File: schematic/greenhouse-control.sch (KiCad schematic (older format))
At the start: 10 parts, among them Q1 BC547, U1 PCF8574

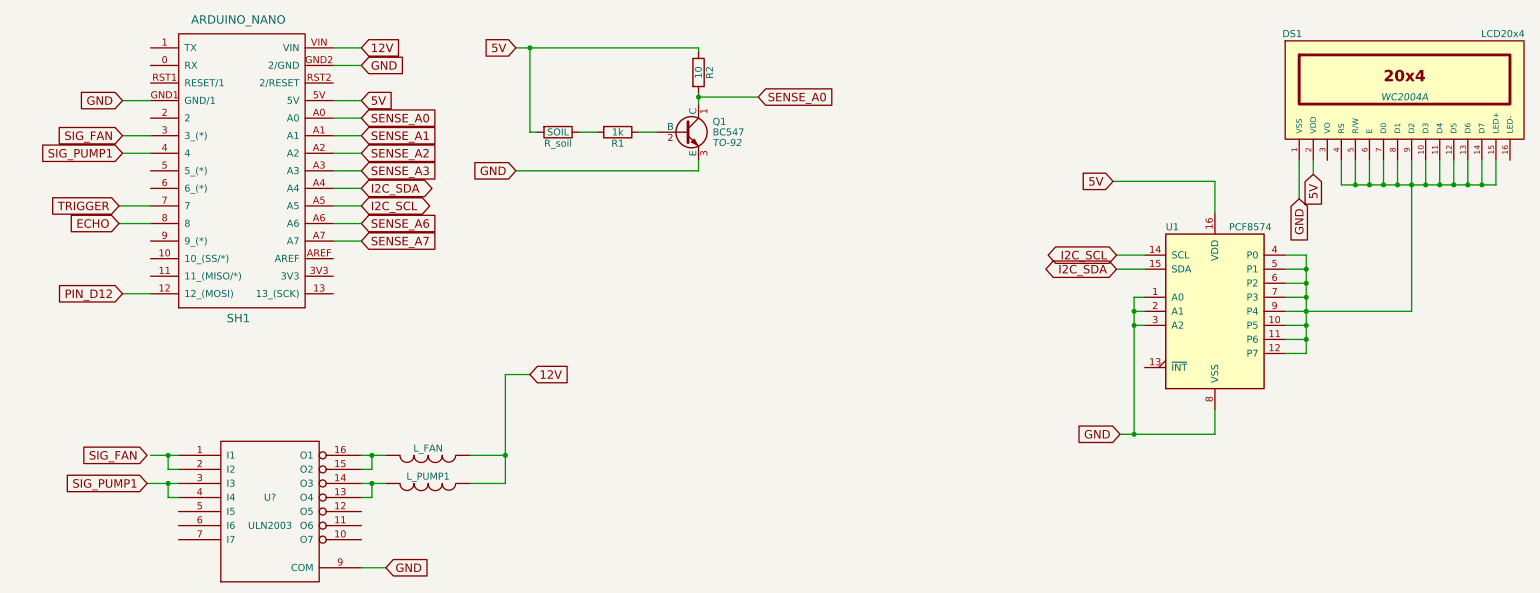
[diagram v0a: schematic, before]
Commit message: Added DHTxx sensor
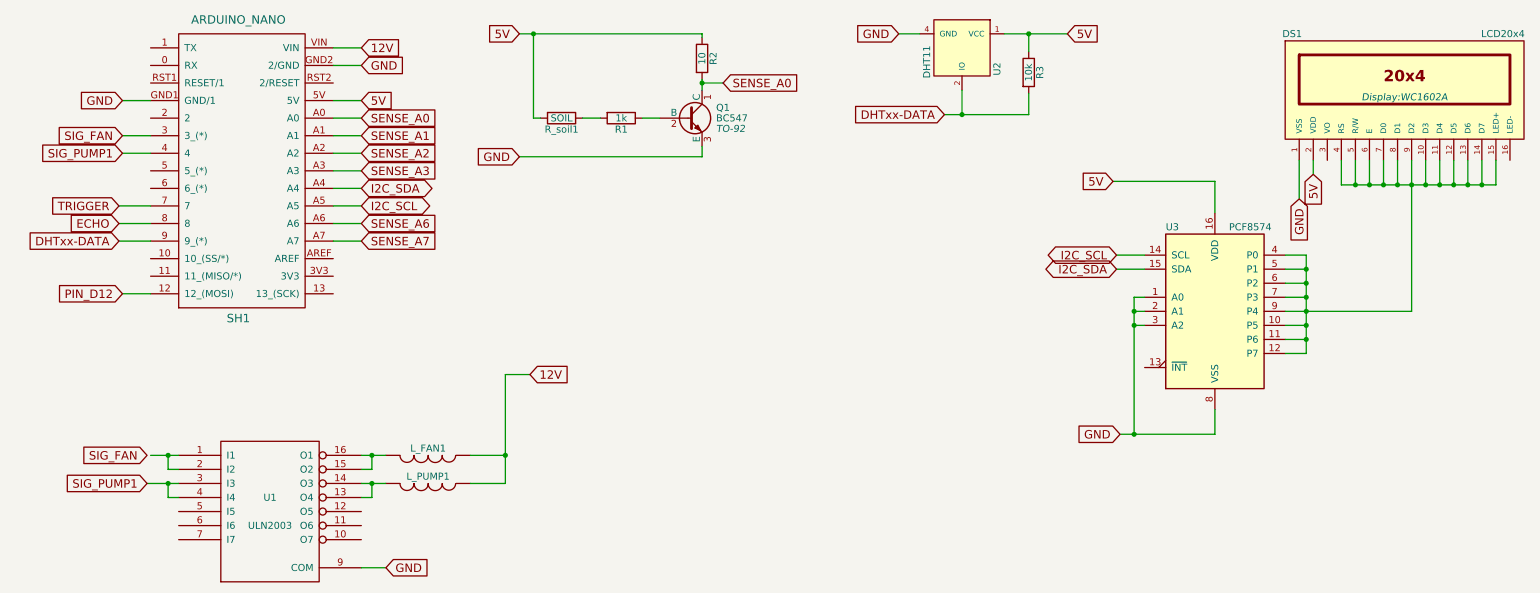
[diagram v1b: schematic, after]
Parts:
- added R3: 10k, symbol R
- added U2: DHT11, symbol DHT11
- DS1: footprint WC2004A -> Display:WC1602A
- gave numbers to parts that had none: 1
- renumbered L_FAN to L_FAN1, R_soil to R_soil1, U1 to U3
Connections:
- net 5V: now also R3.1, U2.1 (VCC)
- net GND: now also U2.4 (GND)
- net DHTxx-DATA: now reaches SH1.9 (9_(*))
- net DHTxx-DATA: now also R3.2, U2.2 (IO)
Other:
- moved on the sheet: Q1, R1, R2, R_soil1
